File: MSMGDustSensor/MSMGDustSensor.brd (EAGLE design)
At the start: 160 x 100 mm, 0 parts

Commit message: schematic almost done
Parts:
- added C1, C2, C3: 0.1uF, MSMG:C0603(1608)
- added D1, D2: MBR120, MSMG:SOD-123
- added J1: POWER_JACK, MSMG:POWER_JACK_PTH
- added JP1: PARTICLE_PHOTON, MSMG:PARTICLE_PHOTON
- added LED1, LED2: LFH1056, MSMG:LFH1056
- added LED3: (no value), MSMG:LED3MM
- added Q1: BC817-16LT1SMD, MSMG:SOT23-BEC
- added R1, R2, R3, R4, R5, R6: (no value), MSMG:R0603(1608)
- added R10, R9: 470, MSMG:R0603(1608)
- added R11, R12, R14, R15, R16, R18: 4.7k, MSMG:R0603(1608)
- added R13, R7, R8: 1k, MSMG:R0603(1608)
- added R17: 47k, MSMG:R0603(1608)
- added S1: (no value), WaterDrop:SKHLACA010
- added TR1, TR2, TR3: DMN2041L, MSMG:SOT23
- added U1: HPMA115S0-XXX, MSMG:HPMA115S0-XXX
- added U2: BUZZER, MSMG:PS1240
- added U3: BME280, MSMG:BME280
- added U4: MCP6002-SO8, MSMG:SO8
- added X1: 53261-0871, MSMG:53261-0871
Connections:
- new net 3.3V: C2.1, JP1.24, R11.2, R12.2, U3.VIN, U4.8
- new net 5V: C1.1, D1.C, D2.C, JP1.1, R1.2, R13.1, R2.2, R3.2, R8.1, S1.P$1, U2.1, X1.2
- new net A0: JP1.12, U4.6, U4.7
- new net A1: JP1.11, U4.1, U4.2
- new net BLUE_LED: JP1.20, R4.2, TR1.1
- new net BUZZER_PWM: JP1.16, R7.2
- new net GND: C1.2, C2.2, C3.2, J1.GND, J1.GNDBREAK, JP1.2, JP1.21, LED3.K, Q1.E, R15.2, R17.2, R4.1, R5.1, R6.1, TR1.2, TR2.2, TR3.2, U3.GND, U4.4, X1.8
- new net GREEN_LED: JP1.19, R5.2, TR2.1
- new net N$1: D1.A, J1.PWR
- new net N$11: R17.1, R18.2, S1.P$2
- new net N$13: Q1.C, R8.2, U2.2
- new net N$14: C3.1, R15.1, R16.2, U4.5
- new net N$15: LED1.R+, LED2.R+, R3.1
- new net N$16: U4.3
- new net N$17: LED3.A, R13.2
- new net N$18: Q1.B, R7.1
- new net N$2: D2.A
- new net N$3: LED1.B+, LED2.B+, R1.1
- new net N$4: LED1.G+, LED2.G+, R2.1
- new net N$5: JP1.3, R9.1
- new net N$6: LED1.B-, LED2.B-, TR1.3
- new net N$7: LED1.G-, LED2.G-, TR2.3
- new net N$8: LED1.R-, LED2.R-, TR3.3
- new net N$9: JP1.4, R10.1
- new net RED_LED: JP1.18, R6.2, TR3.1
- new net RXD: R10.2, X1.6
- new net SCL: JP1.14, R12.1, U3.SCK
- new net SDA: JP1.13, R11.1, U3.SDI
- new net TEST: JP1.17, R18.1
- new net TXD: R9.2, X1.7
- new net VBAT: R16.1
- new net VBAT_: JP1.22
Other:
- board size 160 x 100 mm -> 160 x 134.3 mm

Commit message: schematic almost done
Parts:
- added C4, C5, C6: 0.1uF, MSMG:C0603(1608)
- added J2: (no value), SparkFun-Connectors:1X04
- added U5: TSL2591, MSMG:DFN-6
- added U6: BME280, MSMG:BME280
- R15, R16: value 4.7k -> 47k
- U3: value BME280 -> BME280BOARD; device MSMG:BME280 -> MSMG:BME280BOARD
- moved U3 137.5 mm to (-77.5, -312.4)
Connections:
- net 3.3V: now also C4.1, C5.1, C6.1, J2.1, S1.P$1, U5.5, U6.6, U6.8
- net 5V: no longer S1.P$1
- net GND: now also C4.2, C5.2, C6.2, J2.4, U5.3, U6.1, U6.7
- net SCL: now also J2.2, U5.1, U6.4
- net SDA: now also J2.3, U5.6, U6.3

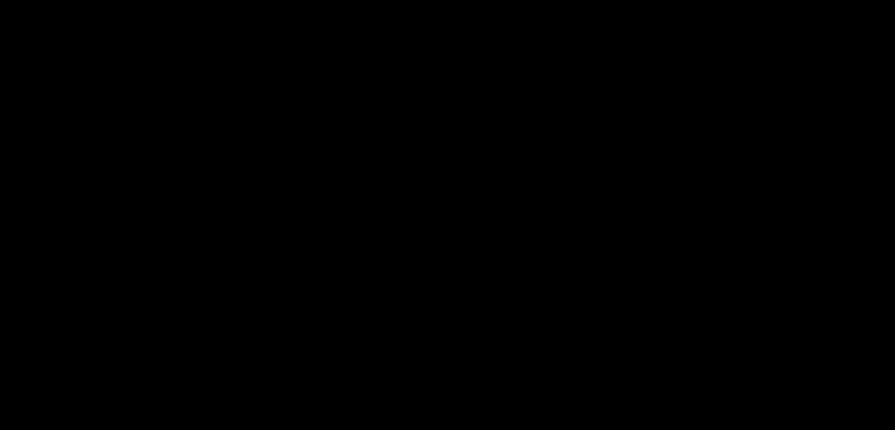
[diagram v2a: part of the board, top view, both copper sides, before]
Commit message: schematic clean up
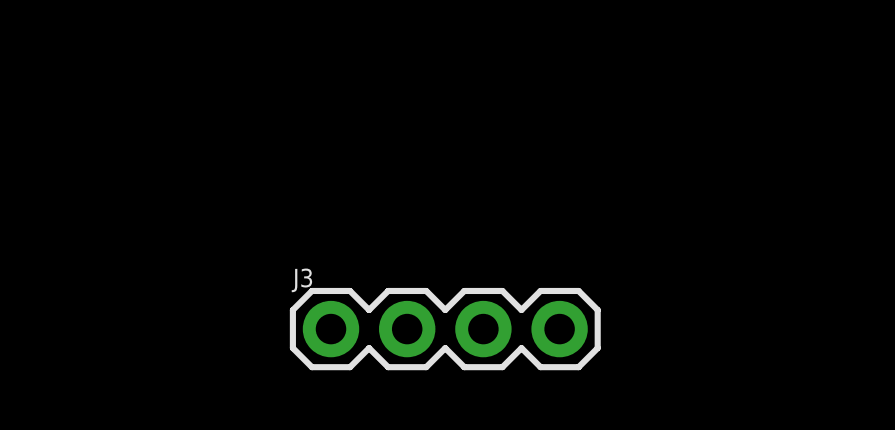
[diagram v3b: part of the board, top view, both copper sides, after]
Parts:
- added J3: (no value), SparkFun-Connectors:1X04
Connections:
- net 5V: now also J3.1
- net GND: now also J3.4
- net N$2: now also J3.3
- net VBAT: now also J3.2
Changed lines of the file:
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@@
 <attribute name="PROD_ID" value="CONN-09696" x="86.36" y="74.93" size="1.778" layer="27" rot="R270" display="off"/>
+</element>
+<element name="J3" library="SparkFun-Connectors" package="1X04" value="" x="-82.55" y="-341.63">
+<attribute name="PROD_ID" value="CONN-09696" x="-82.55" y="-341.63" size="1.778" layer="27" display="off"/>
 </element>
 </elements>
@@
 <contactref element="C6" pad="2"/>
 <contactref element="J2" pad="4"/>
+<contactref element="J3" pad="4"/>
 <wire x1="-74.41" y1="-111.76" x2="-72.91" y2="-127" width="0" layer="19" extent="1-1"/>
 <wire x1="-74.41" y1="-106.68" x2="-74.41" y2="-111.76" width="0" layer="19" extent="1-1"/>
@@
 <wire x1="-89.42" y1="-322.58" x2="-91.195" y2="-315.905" width="0" layer="19" extent="1-1"/>
 <wire x1="-89.42" y1="-328.93" x2="-89.42" y2="-322.58" width="0" layer="19" extent="1-1"/>
+<wire x1="-74.93" y1="-341.63" x2="-89.42" y2="-328.93" width="0" layer="19" extent="1-1"/>
 <wire x1="-26.67" y1="21.67" x2="-72.71" y2="-35.39" width="0" layer="19" extent="1-1"/>
 <wire x1="-21.97" y1="24.67" x2="-26.67" y2="21.67" width="0" layer="19" extent="1-1"/>
 <wire x1="26.67" y1="93.98" x2="-21.97" y2="24.67" width="0" layer="19" extent="1-1"/>
 <wire x1="44.45" y1="88.9" x2="26.67" y2="93.98" width="0" layer="19" extent="1-1"/>
-<wire x1="78.035" y1="51.6" x2="44.45" y2="88.9" width="0" layer="19" extent="1-1"/>
-<wire x1="86.36" y1="67.31" x2="78.035" y2="51.6" width="0" layer="19" extent="1-1"/>
+<wire x1="86.36" y1="67.31" x2="44.45" y2="88.9" width="0" layer="19" extent="1-1"/>
+<wire x1="78.035" y1="51.6" x2="86.36" y2="67.31" width="0" layer="19" extent="1-1"/>
 </signal>
 <signal name="N$1">
@@
 <contactref element="JP1" pad="1"/>
 <contactref element="R13" pad="1"/>
+<contactref element="J3" pad="1"/>
 <wire x1="-74.41" y1="-121.92" x2="-74.41" y2="-127" width="0" layer="19" extent="1-1"/>
 <wire x1="-72.91" y1="-73.66" x2="-74.41" y2="-121.92" width="0" layer="19" extent="1-1"/>
@@
 <wire x1="26.67" y1="96.52" x2="-46.3" y2="-3.81" width="0" layer="19" extent="1-1"/>
 <wire x1="70.535" y1="51.6" x2="26.67" y2="96.52" width="0" layer="19" extent="1-1"/>
+<wire x1="-82.55" y1="-341.63" x2="-84.57" y2="-210.82" width="0" layer="19" extent="1-1"/>
 </signal>
 <signal name="N$2">
 <contactref element="D2" pad="A"/>
+<contactref element="J3" pad="3"/>
+<wire x1="-42.6" y1="-10.16" x2="-77.47" y2="-341.63" width="0" layer="19" extent="1-1"/>
 </signal>
 <signal name="VBAT_">
@@
 <signal name="VBAT">
 <contactref element="R16" pad="1"/>
+<contactref element="J3" pad="2"/>
+<wire x1="-84.57" y1="-229.87" x2="-80.01" y2="-341.63" width="0" layer="19" extent="1-1"/>
 </signal>
 <signal name="BLUE_LED">

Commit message: board file almost done
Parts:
- removed U5: TSL2591, MSMG:DFN-6
- added C7: 0.1uF, MSMG:C0603(1608)
- added H1, H2, H3, H4: MOUNT-PAD-ROUND3.2, holes:3,2-PAD
- added J4, J5, J6: (no value), SparkFun-Connectors:1X04
- added JP2: PARTICLE_PHOTON, MSMG:PARTICLE_PHOTON
- added R19: 1k, MSMG:R0603(1608)
- added X2: 5268-02, OSSI:5628-02
- J1: value POWER_JACK -> (none); device MSMG:POWER_JACK_PTH -> SparkFun-Connectors:1X03
- J2: value (none) -> POWER_JACK; device SparkFun-Connectors:1X04 -> MSMG:POWER_JACK_PTH
- JP1: value PARTICLE_PHOTON -> JP2; device MSMG:PARTICLE_PHOTON -> GFE:JP2SMD0603
- LED1: value LFH1056 -> (none); device MSMG:LFH1056 -> MSMG:LED3MM
- LED3: value (none) -> LFH1056; device MSMG:LED3MM -> MSMG:LFH1056
- R1, R2: value (none) -> 4.7k
- R10, R9: value 470 -> 4.7k
- R11: value 4.7k -> 47k
- R12, R14, R18: value 4.7k -> (none)
- R13: value 1k -> (none)
- R15, R16: value 47k -> (none)
- R17: value 47k -> 1k
- R3, R4: value (none) -> 47k
- R5: value (none) -> 1k
- R6: value (none) -> 470
- R7: value 1k -> 470
- R8: value 1k -> 4.7k
- U1: value HPMA115S0-XXX -> MCP6002-SO8; device MSMG:HPMA115S0-XXX -> MSMG:SO8
- U2: value BUZZER -> TSL2591; device MSMG:PS1240 -> MSMG:DFN-6
- U4: value MCP6002-SO8 -> BME280; device MSMG:SO8 -> MSMG:BME280
- U6: value BME280 -> BUZZER; device MSMG:BME280 -> MSMG:PS1240
- moved C6 369.3 mm to (0.00, 29.2)
- moved C5 361.3 mm to (0.00, 27.3)
- moved U3 334.8 mm to (-8.89, 15.2)
- moved J3 321.7 mm to (3.81, -31.8), turned to 180 degrees
- moved U6 307.8 mm to (-20.3, -16.5), turned to 180 degrees
- moved C4 299.9 mm to (-27.9, 11.4), turned to 90 degrees
- moved R18 285.6 mm to (3.81, 1.27), turned to 90 degrees
- moved R17 276.0 mm to (-12.7, 2.54)
- moved C3 262.7 mm to (22.9, 3.81), turned to 270 degrees
- moved R16 245.9 mm to (0.00, 1.27), turned to 90 degrees
- moved LED3 238.1 mm to (25.4, 17.8), turned to 180 degrees
- moved R15 234.2 mm to (3.81, -6.35), turned to 180 degrees
- moved R14 232.6 mm to (-3.81, 1.27), turned to 90 degrees
- moved S1 224.6 mm to (-20.3, -31.8)
- moved C2 221.5 mm to (19.1, 10.8), turned to 180 degrees
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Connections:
- removed net N$3: LED1.B+, LED2.B+, R1.1
- removed net N$6: LED1.B-, LED2.B-, TR1.3
- removed net N$8: LED1.R-, LED2.R-, TR3.3
- new net B-: J5.2, J6.2, LED2.B-, LED3.B-, R14.2
- new net G-: J5.3, J6.3, LED2.G-, LED3.G-, R16.2
- new net N$10: R14.1, TR1.3
- new net N$12: R16.1, TR2.3
- new net R-: J5.4, J6.4, LED2.R-, LED3.R-, R18.2
- net 3.3V: now also C3.1, J4.1, JP1.3, JP2.24, R8.2, R9.2, U1.8, U2.5, U4.6; no longer C2.1, J2.1, JP1.24, R11.2, R12.2, U5.5, U6.6, U6.8
- net 5V: now also C7.1, J5.1, J6.1, JP2.1, LED2.B+, LED2.G+, LED2.R+, LED3.B+, LED3.G+, LED3.R+, R19.1, R5.1, U6.1; no longer C1.1, R1.2, R13.1, R2.2, R3.2, R8.1, U2.1
- net A0: now also JP2.12, U1.6, U1.7; no longer JP1.12, U4.6, U4.7
- net A1: now also JP2.11, U1.1, U1.2; no longer JP1.11, U4.1, U4.2
- net BLUE_LED: now also JP2.18, R12.2; no longer JP1.20, R4.2
- net BUZZER_PWM: now also JP2.16, R17.2; no longer JP1.16, R7.2
- net GND: now also C7.2, J1.3, J2.GND, J2.GNDBREAK, J4.4, JP2.2, JP2.21, LED1.K, R11.2, R12.1, R13.1, R15.1, R2.2, R4.2, U1.4, U2.3, U4.1, U4.7, X2.2; no longer J1.GND, J1.GNDBREAK, J2.4, JP1.2, JP1.21, LED3.K, R15.2, R17.2, R4.1, R5.1, R6.1, U4.4, U5.3, U6.1, U6.7
- net GREEN_LED: now also JP2.19, R13.2; no longer JP1.19, R5.2
- net N$1: now also J2.PWR, X2.1; no longer J1.PWR
- net N$11: now also R10.2, R11.1; no longer R17.1, R18.2
- net N$13: now also R19.2, U6.2; no longer R8.2, U2.2
- net N$14: now also C2.1, R3.2, R4.1, U1.5; no longer C3.1, R15.1, R16.2, U4.5
- net N$15: now also R18.1, TR3.3; no longer LED1.R+, LED2.R+, R3.1
- net N$16: now also C1.1, R1.2, R2.1, U1.3; no longer U4.3
- net N$17: now also LED1.A, R5.2; no longer LED3.A, R13.2
- net N$18: now also R17.1; no longer R7.1
- net N$4: now also J1.2, R1.1; no longer LED1.G+, LED2.G+, R2.1
- net N$5: now also JP2.3, R6.1; no longer JP1.3, R9.1
- net N$7: now also J1.1, JP1.2; no longer LED1.G-, LED2.G-, TR2.3
- net N$9: now also JP2.4, R7.1; no longer JP1.4, R10.1
- net RED_LED: now also JP2.20, R15.2; no longer JP1.18, R6.2
- net RXD: now also R7.2; no longer R10.2
- net SCL: now also J4.2, JP2.14, R9.1, U2.1, U4.4; no longer J2.2, JP1.14, R12.1, U5.1, U6.4
- net SDA: now also J4.3, JP2.13, R8.1, U2.6, U4.3; no longer J2.3, JP1.13, R11.1, U5.6, U6.3
- net TEST: now also JP2.17, R10.1; no longer JP1.17, R18.1
- net TXD: now also R6.2; no longer R9.2
- net VBAT: now also R3.1; no longer R16.1
- net VBAT_: now also JP2.22; no longer JP1.22
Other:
- board size 160 x 134.3 mm -> 76 x 76 mm

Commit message: almost done
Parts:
- added U$1: MSMG_TEXT, MSMG:MSMG_TEXT
- moved U6 19.9 mm to (-23.5, 3.17), turned to 90 degrees
- moved J4 19.8 mm to (-33.0, 22.9)
- moved C7 18.8 mm to (-33.7, 1.27), turned to 90 degrees
- moved Q1 16.9 mm to (-32.4, 6.35), turned to 180 degrees
- moved R19 15.4 mm to (-31.1, 1.27), turned to 90 degrees
- moved C4 12.7 mm to (-27.9, 24.1)
- moved U2 12.7 mm to (-25.4, 24.1)
- moved LED1 0.63 mm to (12.1, -31.8)
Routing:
- added copper zone on layer 16, net GND
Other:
- outline, holes or cut-outs redrawn
- board text added: "https://msmg.today"

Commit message: gerber done
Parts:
- moved D1 6.63 mm to (0.00, -24.8), turned to 0 degrees
- moved D2 6.38 mm to (0.00, -27.3)
- moved C6 6.35 mm to (3.81, 24.1), turned to 270 degrees
- moved C4 5.08 mm to (-22.9, 24.1), turned to 270 degrees
- turned R6 to 0 degrees
- turned S1 to 180 degrees
- turned U2 to 90 degrees
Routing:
- net 5V: track 0.00 -> 219.8 mm, vias 0 -> 8
- net 3.3V: track 0.00 -> 212.4 mm, vias 0 -> 10
- net SDA: track 0.00 -> 77.8 mm, vias 0 -> 2
- net VBAT: track 0.00 -> 73.1 mm, vias 0 -> 4
- net B-: track 0.00 -> 67.7 mm
- net R-: track 0.00 -> 67.4 mm, vias 0 -> 2
- net G-: track 0.00 -> 66.8 mm, vias 0 -> 2
- net SCL: track 0.00 -> 62.5 mm, vias 0 -> 2
- net N$1: track 0.00 -> 42.9 mm
- net GND: track 0.00 -> 42.6 mm, vias 0 -> 13
- net N$11: track 0.00 -> 38.1 mm
- net N$18: track 0.00 -> 21.5 mm
- net RED_LED: track 0.00 -> 16.9 mm
- net A1: track 0.00 -> 16.5 mm
- net A0: track 0.00 -> 14.5 mm
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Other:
- board text added: "3.3V"
- board text added: "5V"
- board text added: "5Vo"
- board text added: "B"
- board text added: "G"
- board text added: "GND"
- board text added: "R"
- board text added: "SCL"
- board text added: "SDA"
- board text added: "SIG"
- board text added: "TEST"
- board text added: "VBAT"
